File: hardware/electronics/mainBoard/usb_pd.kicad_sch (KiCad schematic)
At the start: 30 parts, among them SW5 4P_SPST, SW6 4P_SPST, U13 TPS25751D

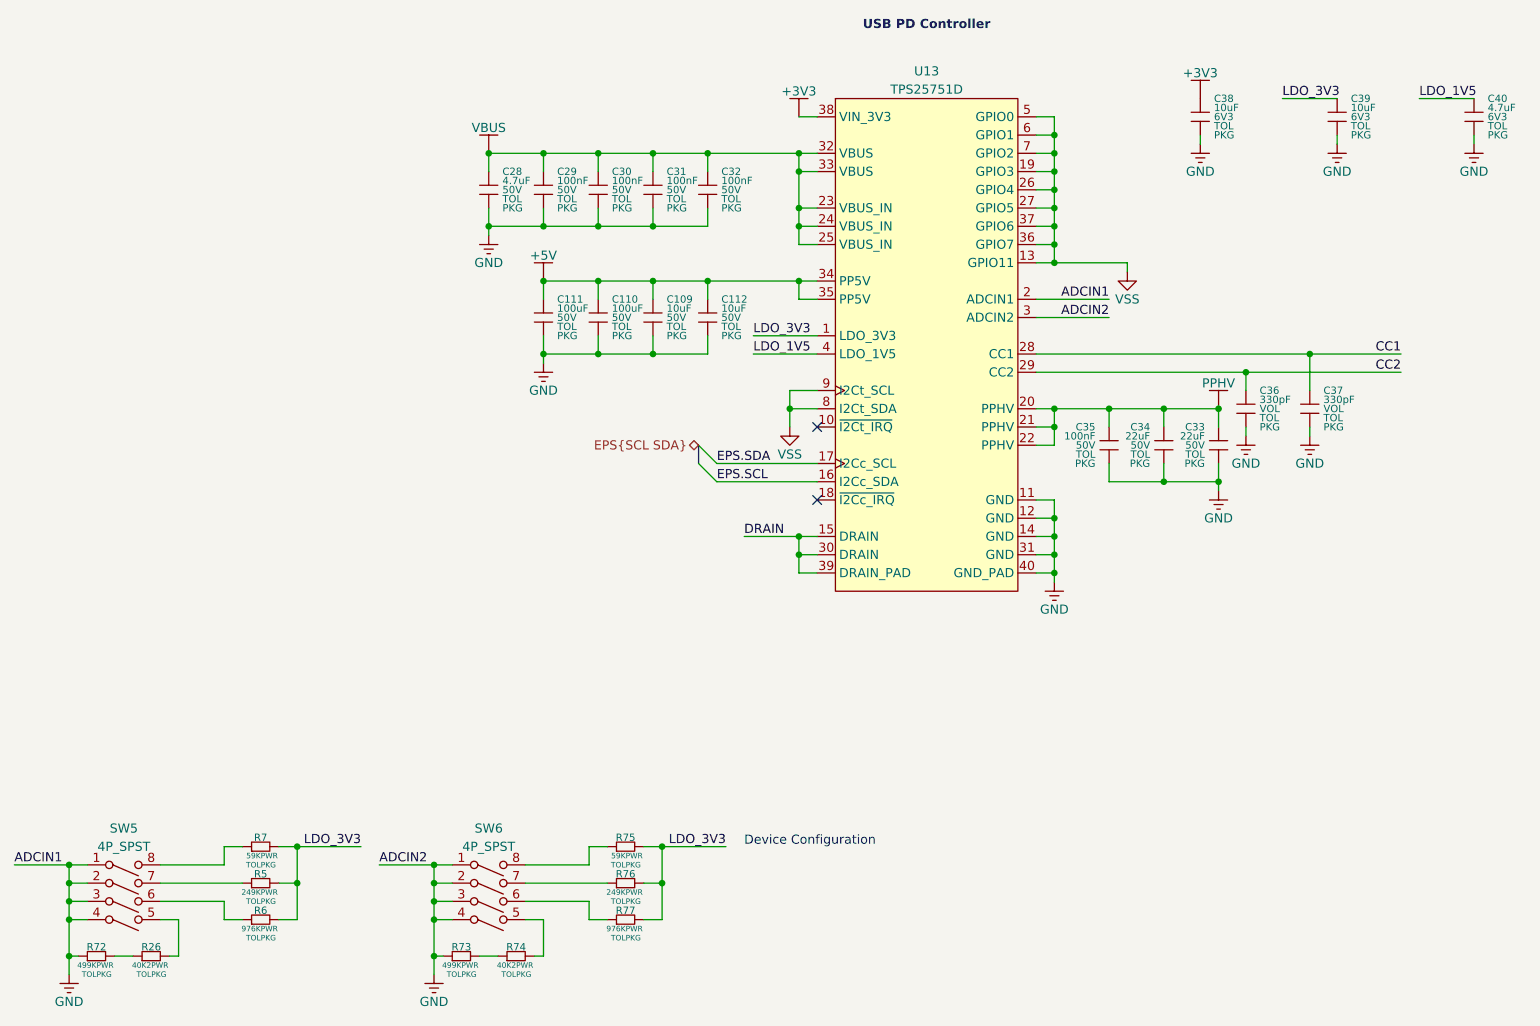
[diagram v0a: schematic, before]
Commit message: replaced capacitors with tants
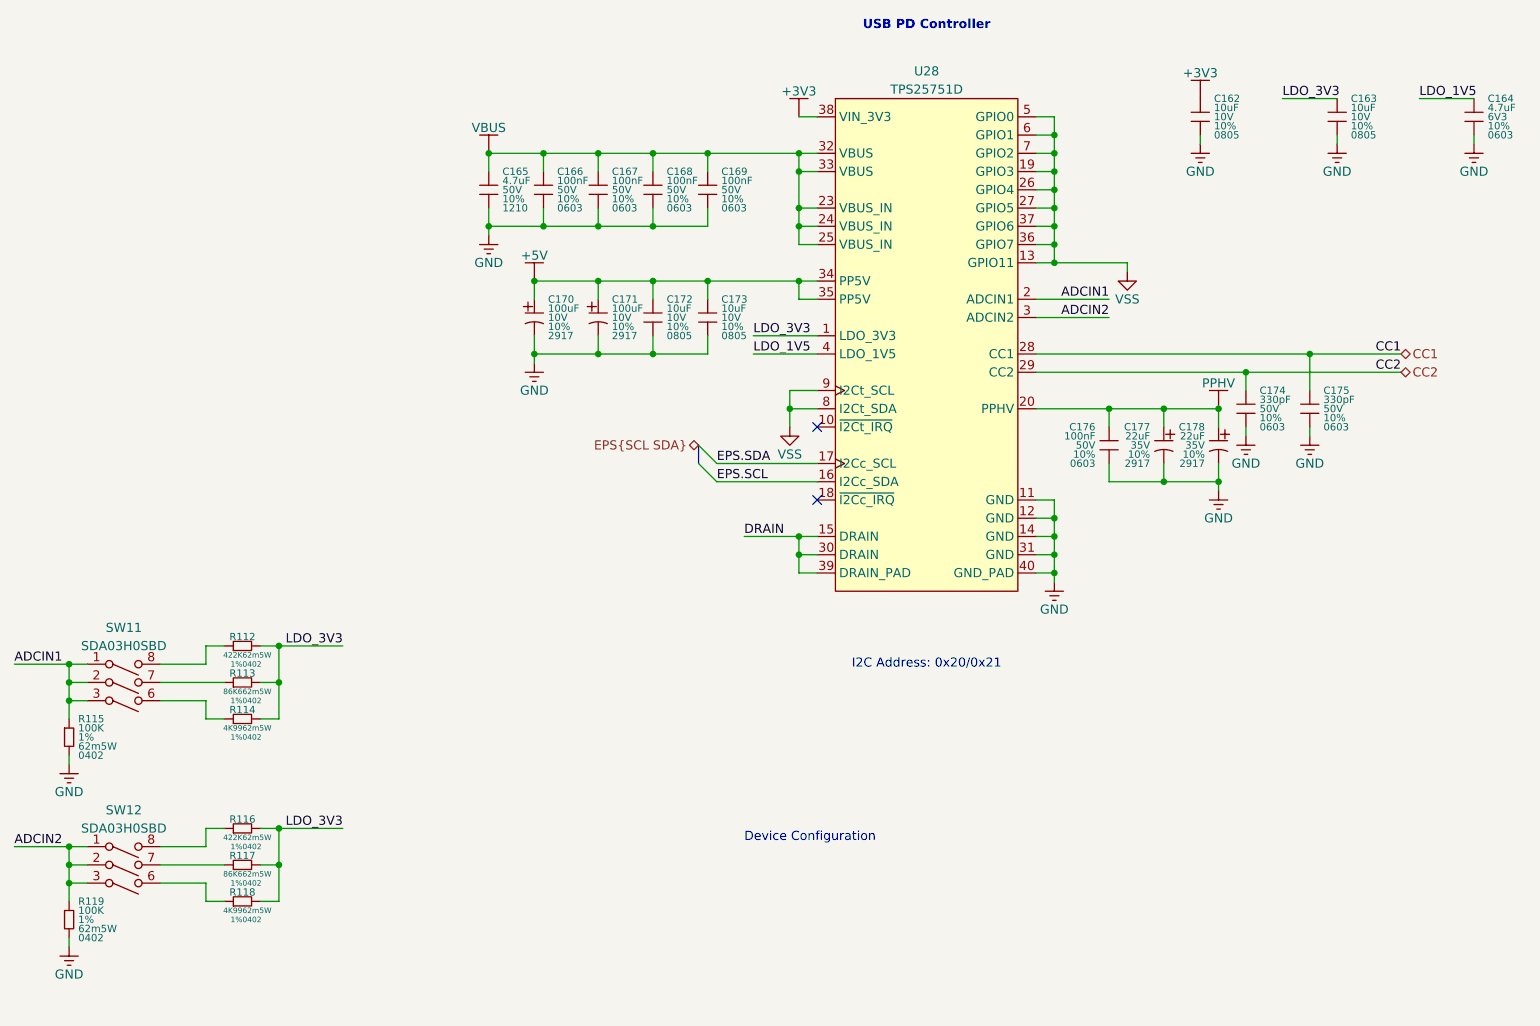
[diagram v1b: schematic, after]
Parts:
- removed C110, C111: 100uF, symbol lib_sch:C
- removed C112, C38, C39: 10uF, symbol lib_sch:C
- removed C29, C30, C31, C32, C35: 100nF, symbol lib_sch:C
- removed C33, C34: 22uF, symbol lib_sch:C
- removed C37: 330pF, symbol lib_sch:C
- removed C40: 4.7uF, symbol lib_sch:C
- removed R26, R74: 40K2, symbol lib_sch:R_horizontal
- removed R5, R76: 249K, symbol lib_sch:R_horizontal
- removed R6, R77: 976K, symbol lib_sch:R_horizontal
- removed R72, R73: 499K, symbol lib_sch:R_horizontal
- removed R75: 59K, symbol lib_sch:R_horizontal
- removed SW5, SW6: 4P_SPST, symbol .DS-Switches:4P_SPST
- added C162, C163, C173: 10uF, symbol lib_sch:C
- added C164: 4.7uF, symbol lib_sch:C
- added C166, C167, C168, C169, C176: 100nF, symbol lib_sch:C
- added C170, C171: 100uF, symbol .DS-Passives:C_polarized
- added C175: 330pF, symbol lib_sch:C
- added C177, C178: 22uF, symbol .DS-Passives:C_polarized
- added R113, R117: 86K6, symbol lib_sch:R_horizontal
- added R114, R118: 4K99, symbol lib_sch:R_horizontal
- added R115, R119: 100K, symbol lib_sch:R
- added R116: 422K, symbol lib_sch:R_horizontal
- added SW11, SW12: SDA03H0SBD, symbol .DS-Switches:3P_SPST
- C165: renamed from C28; DKPN (none) -> 490-8066-1-ND; MPN (none) -> GCM32ER71H475KA55K; Manufacturer (none) -> Murata Electronics; Package PKG -> 1210; Tolerance TOL -> 10%
- C172: renamed from C109; DKPN (none) -> 490-10674-1-ND; MPN (none) -> GCM21BR71A106KE22L; Manufacturer (none) -> Murata Electronics; Package PKG -> 0805; Tolerance TOL -> 10%; Voltage Rating 50V -> 10V
- C174: renamed from C36; DKPN (none) -> 478-06035C331K4T2ACT-ND; MPN (none) -> 06035C331K4T2A; Manufacturer (none) -> KYOCERA AVX; Package PKG -> 0603; Tolerance TOL -> 10%; Voltage Rating VOL -> 50V
- R112: renamed from R7; value 59K -> 422K; DKPN (none) -> 541-422KLCT-ND; MPN (none) -> CRCW0402422KFKED; Manufacturer (none) -> Vishay Dale; Package PKG -> 0402; Power Rating PWR -> 62m5W; Tolerance TOL -> 1%
- U28: renamed from U13; symbol .DS-PMIC:TPS25751D -> lib_sch:TPS25751D
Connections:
- net +3V3: now also C162.1
- net +5V: now also C170.1, C171.1, C173.1
- net CC1: now also C175.1
- net GND: now also C162.2, C163.2, C164.2, C166.2, C167.2, C168.2, C169.2, C170.2, C171.2, C173.2, C175.2, C176.2, C177.2, C178.2, R115.2, R119.2; no longer U28.2 (ADCIN1), U28.3 (ADCIN2)
- net LDO_1V5: now also C164.1
- net LDO_3V3: now also C163.1, R113.2, R114.2, R116.2, R117.2, R118.2
- net PPHV: now also C176.1, C177.1, C178.1
- net VBUS: now also C166.1, C167.1, C168.1, C169.1
- net at R112.1: now also SW11.8
- new net: R116.1, SW12.8
- new net: R114.1, SW11.6
- new net: R113.1, SW11.7
- new net: R118.1, SW12.6
- new net: R117.1, SW12.7
- new net ADCIN1: R115.1, SW11.1, SW11.2, SW11.3, U28.2 (ADCIN1)
- new net ADCIN2: R119.1, SW12.1, SW12.2, SW12.3, U28.3 (ADCIN2)
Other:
- note added: "I2C Address: 0x20/0x21"
- moved on the sheet: R112
